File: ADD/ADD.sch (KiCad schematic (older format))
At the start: 11 parts, among them J1 Conn_01x08_Male, J2 Conn_01x08_Male, J3 Conn_01x08_Male, J4 Conn_01x05_Male, U1 74LS283, U2 74LS283, U3 74LS573

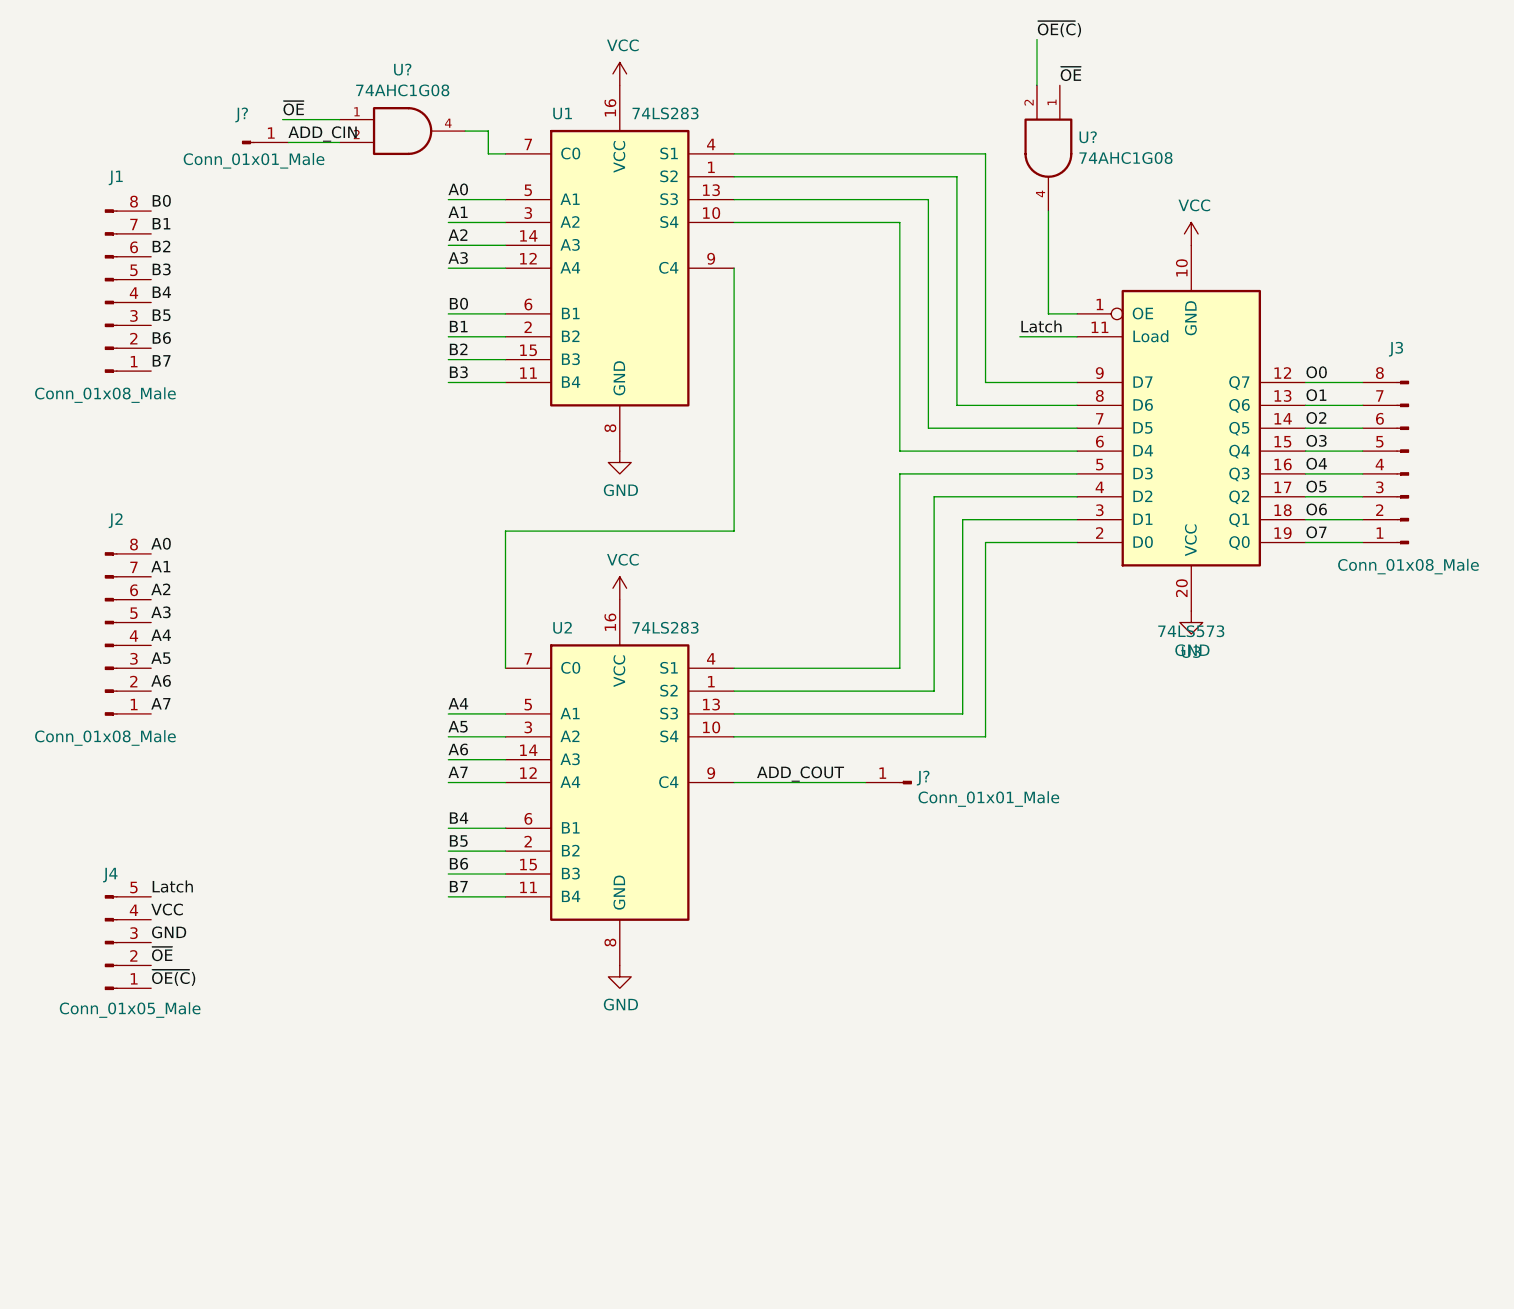
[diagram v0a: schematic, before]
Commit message: Polishing ADD cmd
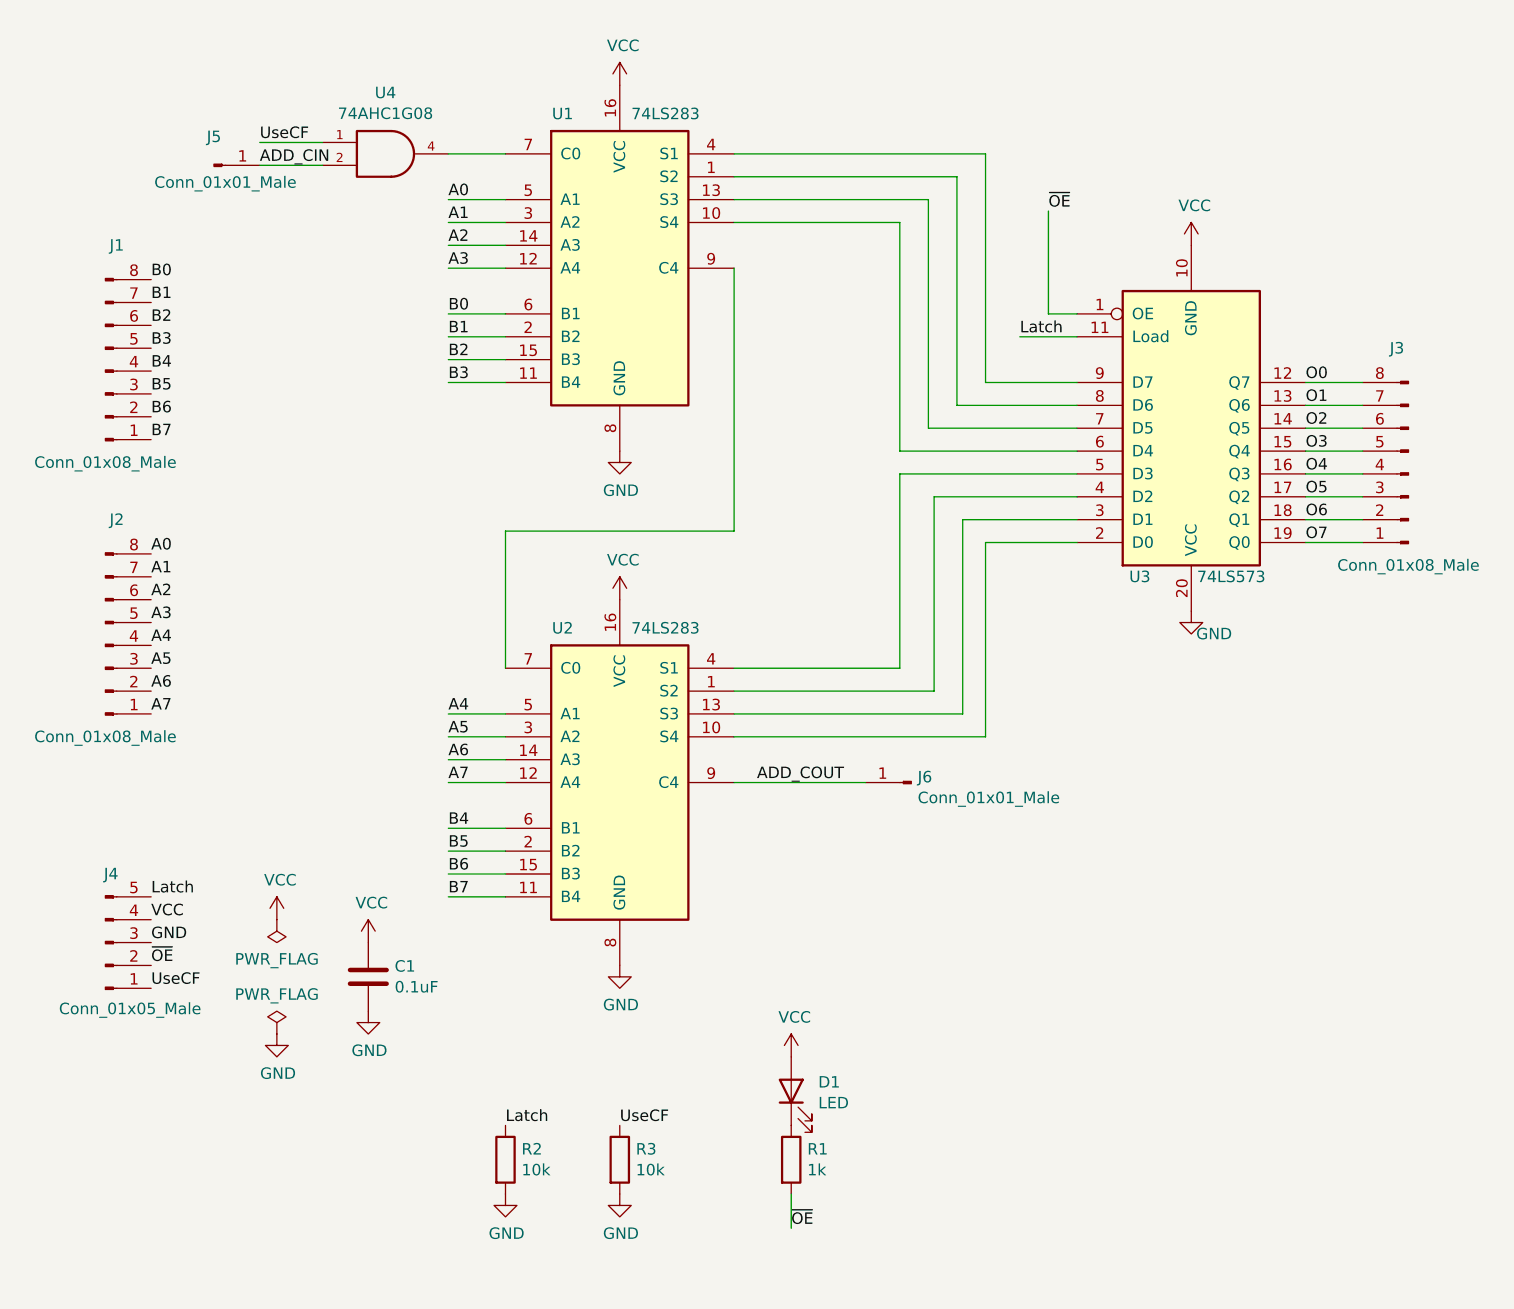
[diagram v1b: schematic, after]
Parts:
- removed U?: 74AHC1G08, symbol 74xGxx:74AHC1G08
- added C1: 0.1uF, Capacitor_SMD:C_0805_2012Metric_Pad1.18x1.45mm_HandSolder, symbol Device:C
- added D1: LED, LED_SMD:LED_0805_2012Metric_Pad1.15x1.40mm_HandSolder, symbol Device:LED
- added R1: 1k, Resistor_SMD:R_0805_2012Metric_Pad1.20x1.40mm_HandSolder, symbol Device:R
- added R2, R3: 10k, Resistor_SMD:R_0805_2012Metric_Pad1.20x1.40mm_HandSolder, symbol Device:R
- J5, J6: renamed from J?; footprint (none) -> Connector_PinHeader_2.54mm:PinHeader_1x01_P2.54mm_Vertical
- U4: renamed from U?; footprint (none) -> CommonLibrary:tssop5
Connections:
- net GND: now also C1.2, R2.2, R3.2
- net Latch: now also R2.1
- net VCC: now also C1.1, D1.2 (A)
- net ~OE: now also U3.1 (OE), R1.2; no longer U4.1
- net ~OE(C) renamed UseCF
- net UseCF: now also U4.1, R3.1
- new net: D1.1 (K), R1.1
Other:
- moved on the sheet: J1, J5, U4

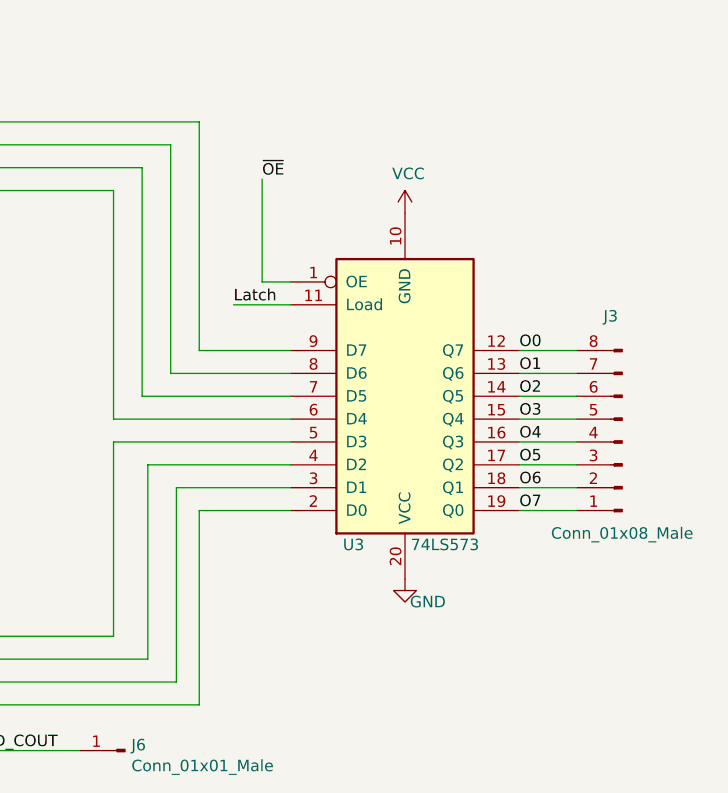
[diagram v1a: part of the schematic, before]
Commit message: Epic fail. Fix power supply on ADD.
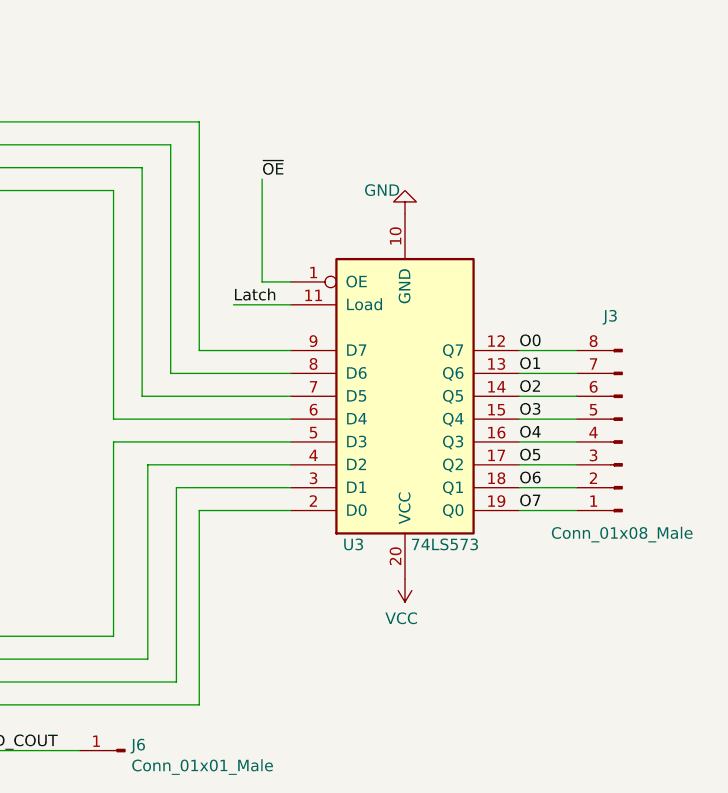
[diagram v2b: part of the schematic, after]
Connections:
- net GND: now also U3.10 (GND); no longer U3.20 (VCC)
- net VCC: now also U3.20 (VCC); no longer U3.10 (GND)
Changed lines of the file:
@@
 L power:GND #PWR04
 U 1 1 62B2EF0E
-P 5750 3750
-F 0 "#PWR04" H 5750 3500 50  0001 C CNN
-F 1 "GND" H 5850 3650 50  0000 C CNN
-F 2 "" H 5750 3750 50  0001 C CNN
-F 3 "" H 5750 3750 50  0001 C CNN
-	1    5750 3750
-	1    0    0    -1
+P 5750 2150
+F 0 "#PWR04" H 5750 1900 50  0001 C CNN
+F 1 "GND" H 5850 2050 50  0000 C CNN
+F 2 "" H 5750 2150 50  0001 C CNN
+F 3 "" H 5750 2150 50  0001 C CNN
+	1    5750 2150
+	-1   0    0    1
 $EndComp
 $Comp
@@
 L power:VCC #PWR02
 U 1 1 62B30B45
-P 5750 2150
-F 0 "#PWR02" H 5750 2000 50  0001 C CNN
-F 1 "VCC" H 5765 2323 50  0000 C CNN
-F 2 "" H 5750 2150 50  0001 C CNN
-F 3 "" H 5750 2150 50  0001 C CNN
-	1    5750 2150
-	1    0    0    -1
+P 5750 3750
+F 0 "#PWR02" H 5750 3600 50  0001 C CNN
+F 1 "VCC" H 5765 3923 50  0000 C CNN
+F 2 "" H 5750 3750 50  0001 C CNN
+F 3 "" H 5750 3750 50  0001 C CNN
+	1    5750 3750
+	-1   0    0    1
 $EndComp
 $Comp
